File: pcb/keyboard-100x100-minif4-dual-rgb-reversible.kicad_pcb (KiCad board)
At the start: 2 copper layers, 100 x 100 mm, 110 parts, among them J1 TRRS, J2 TRRS, J3 Conn_01x04_Female, M1 Motor_DC, Q1 Q_NPN_BCE, U1 BluePill_or_MiniF4, U2 SN74LVC1T45DBV

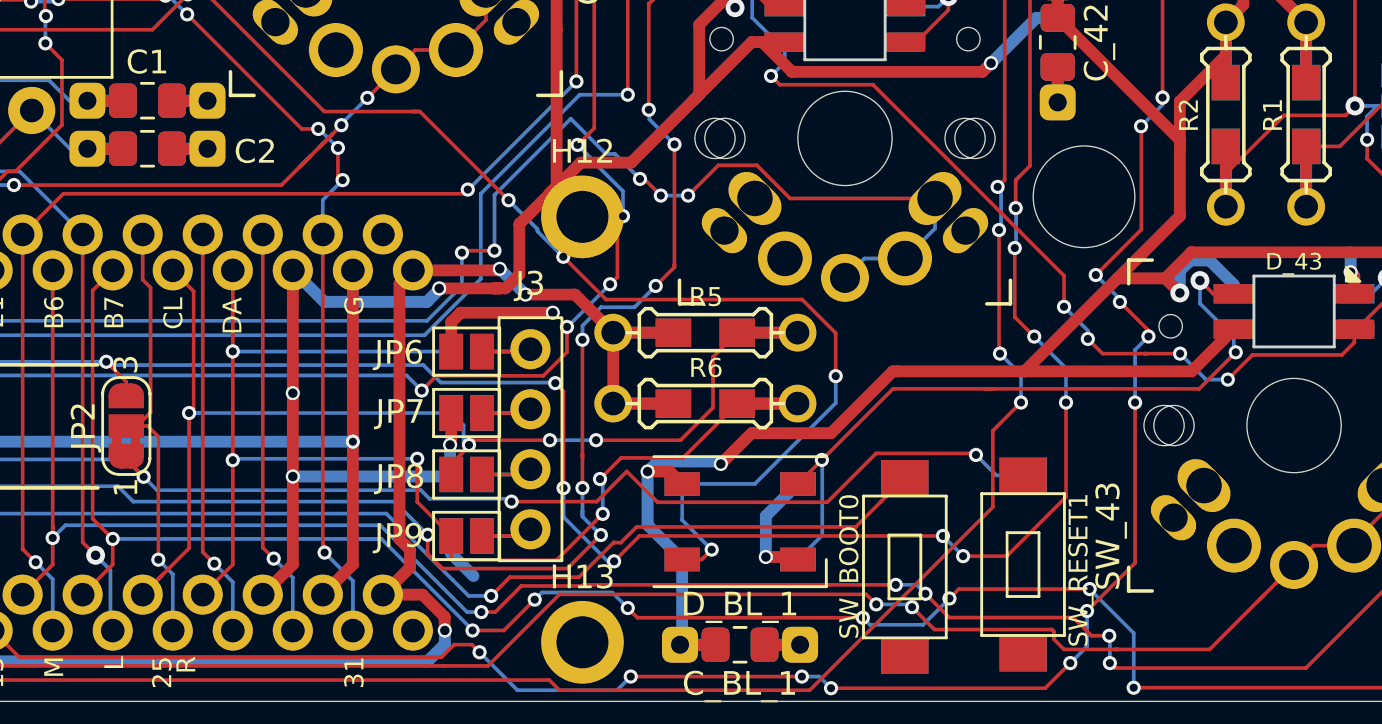
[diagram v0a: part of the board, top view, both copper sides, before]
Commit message: pullup OLED CL/DA to simplify routing; adjust OLED JPs
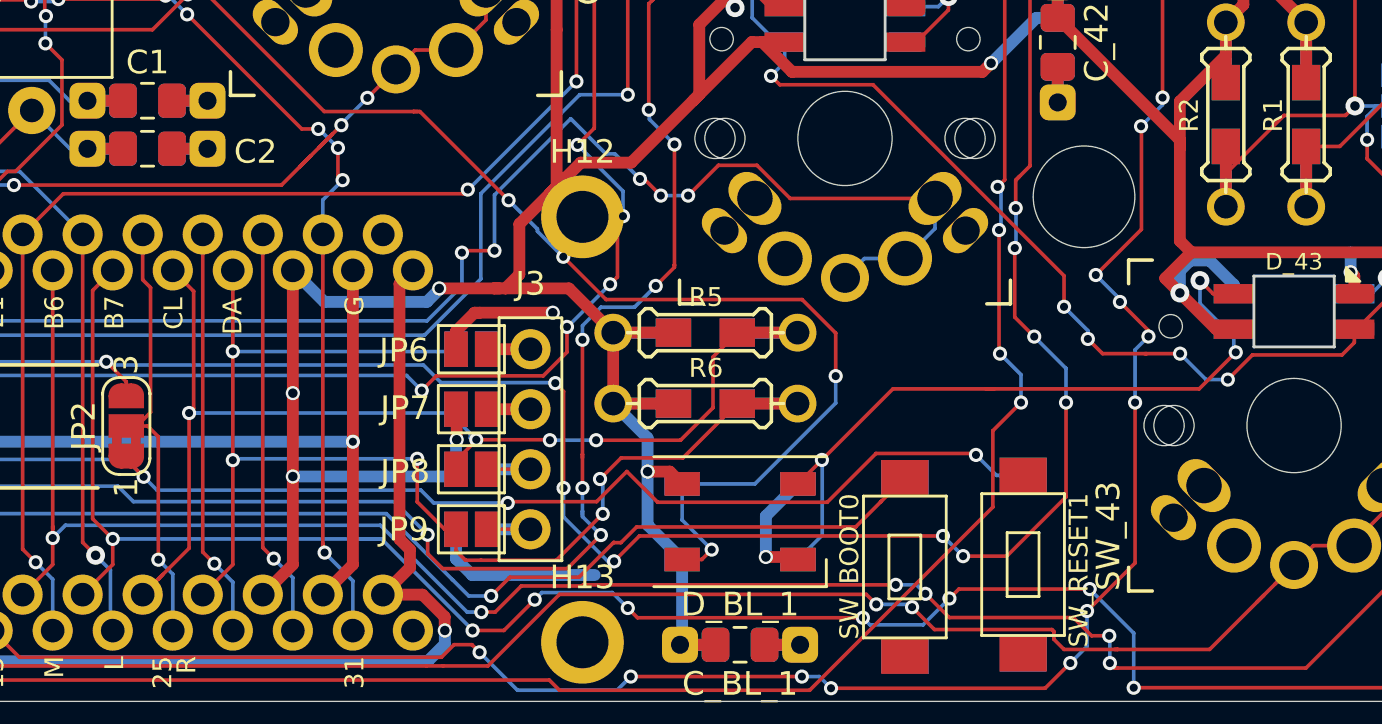
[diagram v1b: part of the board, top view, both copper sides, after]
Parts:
- moved JP10 0.34 mm to (154.8, 142.7)
- moved JP9 0.34 mm to (154.8, 142.7)
- moved JP11 0.30 mm to (154.8, 140.2)
- moved JP8 0.30 mm to (154.8, 140.2)
- moved JP12 0.26 mm to (154.8, 137.6)
- moved JP7 0.26 mm to (154.8, 137.6)
- moved JP13 0.22 mm to (154.8, 135.1)
- moved JP6 0.22 mm to (154.8, 135.1)
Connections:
- R5 pad 1: /3V3 -> /5V
- R6 pad 1: /3V3 -> /5V
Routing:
- net /5V: track 1016.4 -> 994.5 mm, vias 37 -> 36
- net /3V3: track 127.1 -> 114.4 mm, vias 4 -> 2
- net /GND: track 204.0 -> 208.7 mm
- net Net-(J3-Pad4): track 4.33 -> 3.70 mm
- net Net-(J3-Pad3): track 4.28 -> 3.70 mm
- net Net-(J3-Pad2): track 4.23 -> 3.70 mm

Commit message: everything connected; albeit very untidy
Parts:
- moved C_BL_1 9.04 mm to (164.7, 138.7)
- moved R6 0.88 mm to (164.7, 136.5)
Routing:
- net /GND: track 208.7 -> 229.8 mm, vias 46 -> 48
- net /5V: track 994.5 -> 990.1 mm, vias 36 -> 35
- net /OLED_SDA: track 52.3 -> 53.4 mm

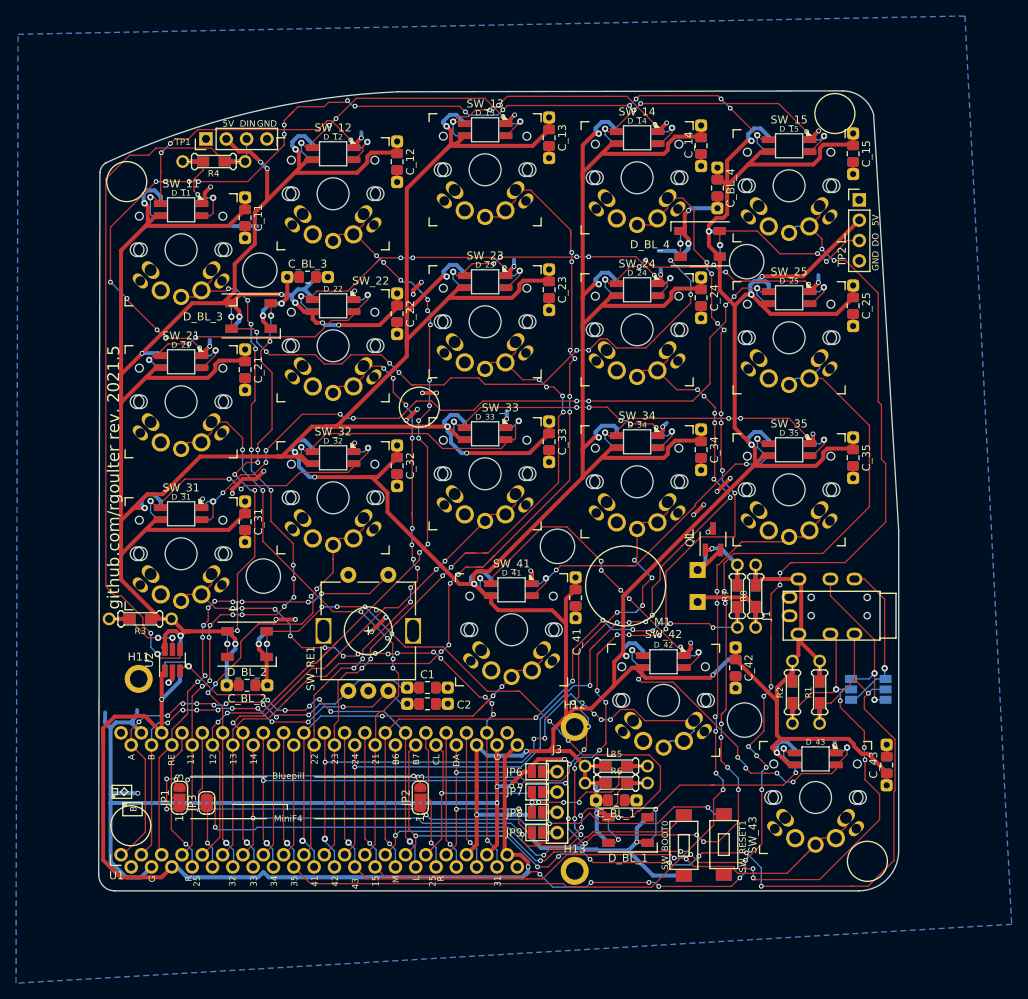
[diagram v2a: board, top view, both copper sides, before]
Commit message: wip; move resistor pairs so they all look similar distance apart;
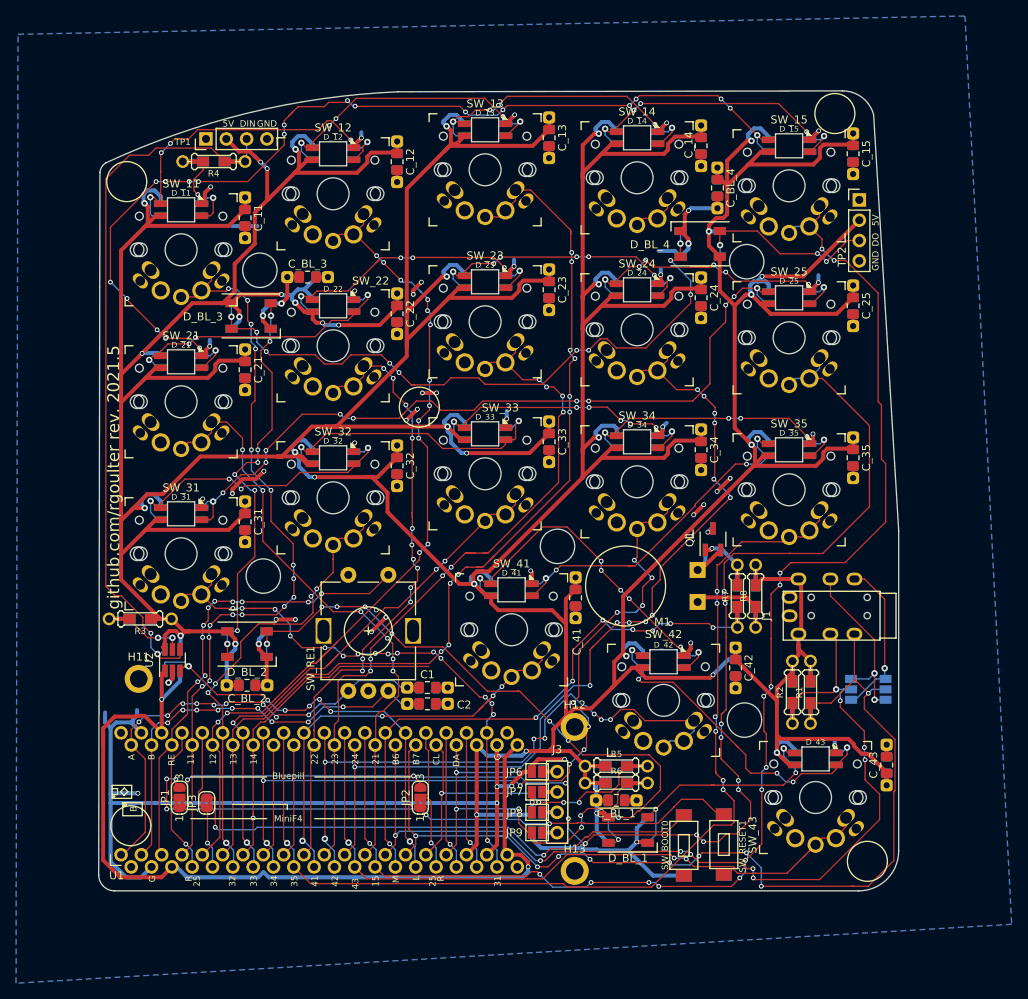
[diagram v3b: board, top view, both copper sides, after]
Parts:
- moved R1 1.14 mm to (189.0, 125.2)
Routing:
- net /SW14: track 165.2 -> 47.4 mm, vias 20 -> 1
- net /SW35: track 124.2 -> 126.8 mm
- net /SW25: track 165.3 -> 167.3 mm
- net /SW15: track 171.4 -> 170.0 mm, vias 17 -> 15
- net /5V: track 990.1 -> 988.7 mm
- net /SDA_RX: track 122.9 -> 124.0 mm
- net /SW13: track 124.8 -> 125.8 mm
- net /SW23: track 89.8 -> 90.7 mm
- net /SW22: track 79.6 -> 80.3 mm
- net Net-(D_42-Pad2): track 43.0 -> 43.3 mm, vias 7 -> 5
- net /RESET: track 80.0 -> 79.8 mm, vias 6 -> 5

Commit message: technically everything connected
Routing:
- net /SW14: track 47.4 -> 118.1 mm, vias 1 -> 11
- net /SW13: track 125.8 -> 121.7 mm

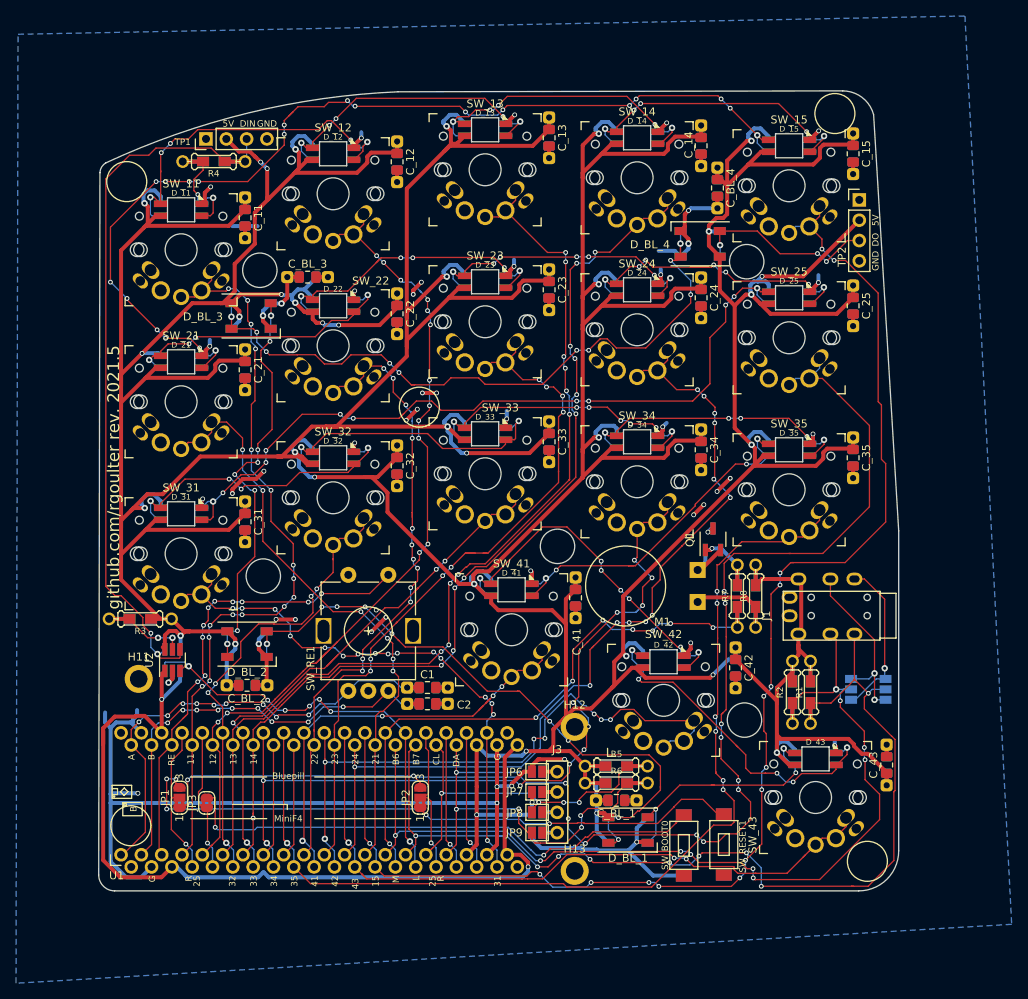
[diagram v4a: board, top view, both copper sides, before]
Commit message: remove all SW_xx traces; clean around H12
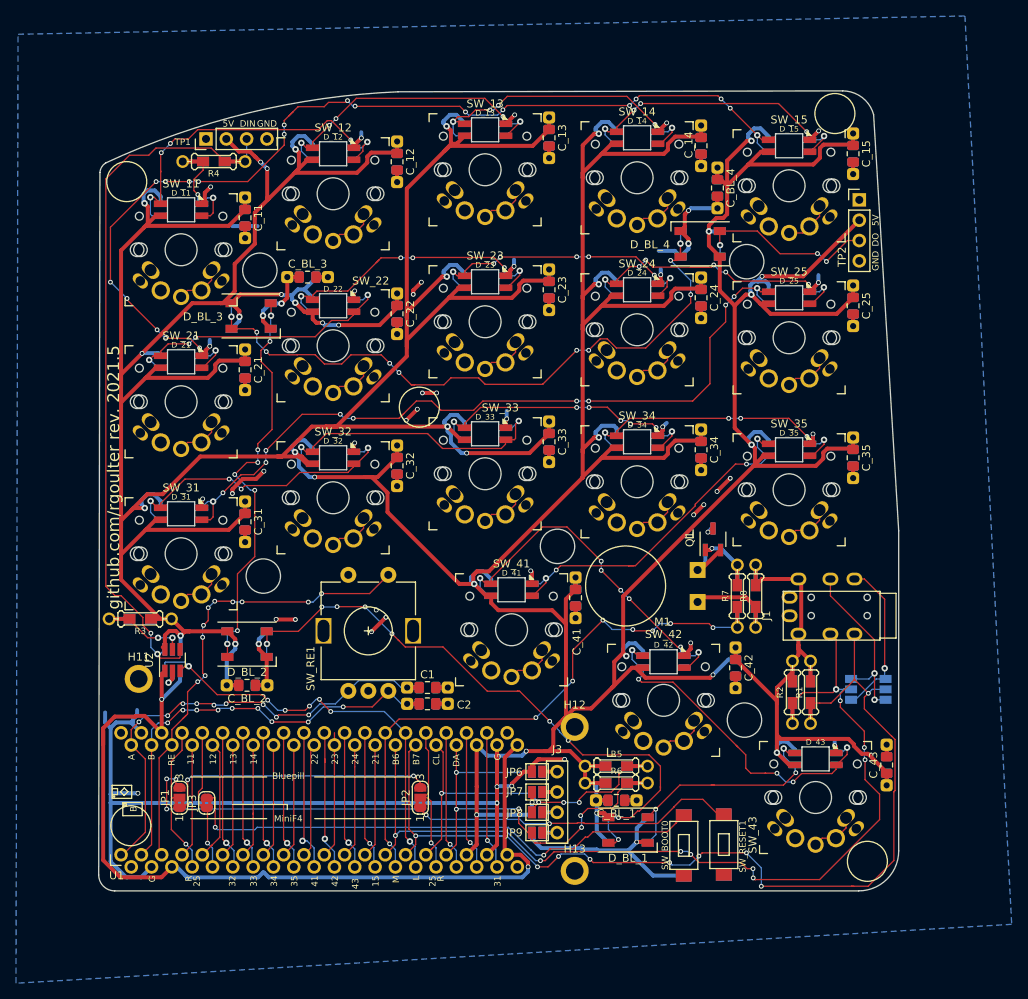
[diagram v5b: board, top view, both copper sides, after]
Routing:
- net /SW15: track 170.0 -> 23.2 mm, vias 15 -> 1
- net /SW25: track 167.3 -> 40.4 mm, vias 13 -> 2
- net /SW35: track 126.8 -> 23.3 mm, vias 7 -> 1
- net /SW13: track 121.7 -> 20.2 mm, vias 10 -> 0
- net /SW14: track 118.1 -> 20.3 mm, vias 11 -> 0
- net /SW24: track 110.4 -> 20.3 mm, vias 12 -> 0
- net /SW12: track 110.1 -> 21.2 mm, vias 14 -> 0
- net /SW34: track 101.8 -> 23.2 mm, vias 11 -> 1
- net /SW11: track 94.7 -> 20.2 mm, vias 16 -> 0
- net /SW23: track 90.7 -> 21.8 mm, vias 8 -> 0
- net /SW43: track 87.4 -> 23.3 mm, vias 3 -> 1
- net /SW22: track 80.3 -> 20.5 mm, vias 12 -> 0
- net /SW21: track 75.0 -> 20.3 mm, vias 6 -> 0
- net /SW42: track 77.8 -> 23.5 mm, vias 7 -> 1
- net /SW33: track 71.0 -> 23.3 mm, vias 4 -> 1
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
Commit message: wip, retracing
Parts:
- moved R3 2.62 mm to (107.8, 116.1)
- moved C_BL_3 1.14 mm to (127.3, 73.3)
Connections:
- U1 pad 1: /RE_A -> /SW11
- U1 pad 10: /SW22 -> /SW24
- U1 pad 11: /SW23 -> /RE_A
- U1 pad 12: /SW24 -> /SW42
- U1 pad 13: /SW21 -> /SW43
- U1 pad 2: /RE_B -> /SW21
- U1 pad 21: (no net) -> /GND_or_5V
- U1 pad 27: /SW33 -> /RGB_DIN_3V3
- U1 pad 28: /SW34 -> /SW_RE
- U1 pad 29: /SW35 -> /SW33
- U1 pad 3: /SW_RE -> /SW31
- U1 pad 30: /SW41 -> /SW14
- U1 pad 31: /SW42 -> /SW34
- U1 pad 32: /SW43 -> /RE_B
- U1 pad 35: /RGB_DIN_3V3 -> /SW35
- U1 pad 39: /SW31 -> /SW41
- U1 pad 4: /SW11 -> /SW12
- U1 pad 40: (no net) -> Net-(U1-Pad40)
- U1 pad 5: /SW12 -> /SW22
- U1 pad 7: /SW14 -> /SW23
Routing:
- net /SW14: track 20.3 -> 111.4 mm, vias 0 -> 13
- net /SW13: track 20.2 -> 105.8 mm, vias 0 -> 16
- net /SW12: track 21.2 -> 96.0 mm, vias 0 -> 12
- net /SW24: track 20.3 -> 93.6 mm, vias 0 -> 8
- net /SW11: track 20.2 -> 84.9 mm, vias 0 -> 8
- net /SW34: track 23.2 -> 86.2 mm, vias 1 -> 7
- net /SW23: track 21.8 -> 81.2 mm, vias 0 -> 9
- net /SW22: track 20.5 -> 74.1 mm, vias 0 -> 4
- net /SW21: track 20.3 -> 69.7 mm, vias 0 -> 6
- net /SW33: track 23.3 -> 60.2 mm, vias 1 -> 5
- net /SW32: track 23.4 -> 53.3 mm, vias 1 -> 3
- net /RE_A: track 56.9 -> 30.7 mm, vias 9 -> 0
- net /RE_B: track 52.3 -> 29.6 mm, vias 9 -> 1
- net /RGB_DIN_3V3: track 55.1 -> 35.2 mm, vias 7 -> 5
- net /SW31: track 23.5 -> 41.0 mm, vias 1 -> 2
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
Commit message: retraced, but some still needs some tidying
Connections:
- U1 pad 11: /RE_A -> /SW15
- U1 pad 12: /SW42 -> /RE_B
- U1 pad 13: /SW43 -> /SW35
- U1 pad 21: /GND_or_5V -> (no net)
- U1 pad 32: /RE_B -> /RE_A
- U1 pad 33: /SW15 -> /SW41
- U1 pad 35: /SW35 -> /SW42
- U1 pad 39: /SW41 -> /SW43
- U1 pad 40: Net-(U1-Pad40) -> (no net)
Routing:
- net /SW15: track 23.2 -> 134.5 mm, vias 1 -> 18
- net /SW25: track 40.4 -> 142.1 mm, vias 2 -> 15
- net /SW35: track 23.2 -> 86.1 mm, vias 1 -> 6
- net /SW43: track 20.3 -> 68.7 mm, vias 0 -> 3
- net /SW42: track 20.3 -> 66.6 mm, vias 0 -> 7
- net /SW41: track 23.5 -> 48.7 mm, vias 1 -> 2
- net /SW14: track 111.4 -> 116.2 mm
- net /RE_B: track 29.6 -> 25.9 mm, vias 1 -> 0
- net /SW23: track 81.2 -> 84.8 mm
- net /SW13: track 105.8 -> 109.2 mm
- net /SW33: track 60.2 -> 63.3 mm
- net /SW_RE: track 43.5 -> 46.5 mm
- net /SW34: track 86.2 -> 83.8 mm
- net /SDA_RX: track 124.0 -> 121.6 mm, vias 9 -> 3
- net /GND: track 216.2 -> 213.9 mm, vias 37 -> 32
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
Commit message: more tidying
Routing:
- net /BOOT0: track 67.1 -> 78.3 mm, vias 2 -> 3
- net /GND: track 213.9 -> 221.5 mm, vias 32 -> 34
- net /SDA_RX: track 121.6 -> 115.9 mm
- net /SW21: track 69.7 -> 65.1 mm
- net /SCL_TX: track 118.3 -> 114.2 mm
- net Net-(D_41-Pad2): track 45.4 -> 41.5 mm
- net /SW35: track 86.1 -> 89.2 mm, vias 6 -> 8
- net /MOTOR_PWM: track 68.5 -> 71.5 mm, vias 10 -> 9
- net /RESET: track 79.8 -> 82.7 mm, vias 5 -> 6
- net /SW13: track 109.2 -> 106.6 mm, vias 16 -> 14
- net /RE_A: track 31.1 -> 33.1 mm, vias 1 -> 2
- net Net-(D_BL_3-Pad4): track 83.0 -> 84.8 mm, vias 10 -> 12
- net /SW23: track 84.8 -> 86.6 mm, vias 9 -> 8
- net /SW25: track 142.1 -> 140.5 mm
- net Net-(D_34-Pad2): track 36.3 -> 37.9 mm
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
